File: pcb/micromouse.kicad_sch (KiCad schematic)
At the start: 15 parts, among them J1 AVR-ISP-6, U1 TSSP77038ETR, U2 TSSP77038ETR, U3 TSSP77038ETR, U4 TSSP77038ETR, U5 TSSP77038ETR, U6 TSSP77038ETR, U7 ATmega328PB-A, U8 MX1508, Y1 Crystal

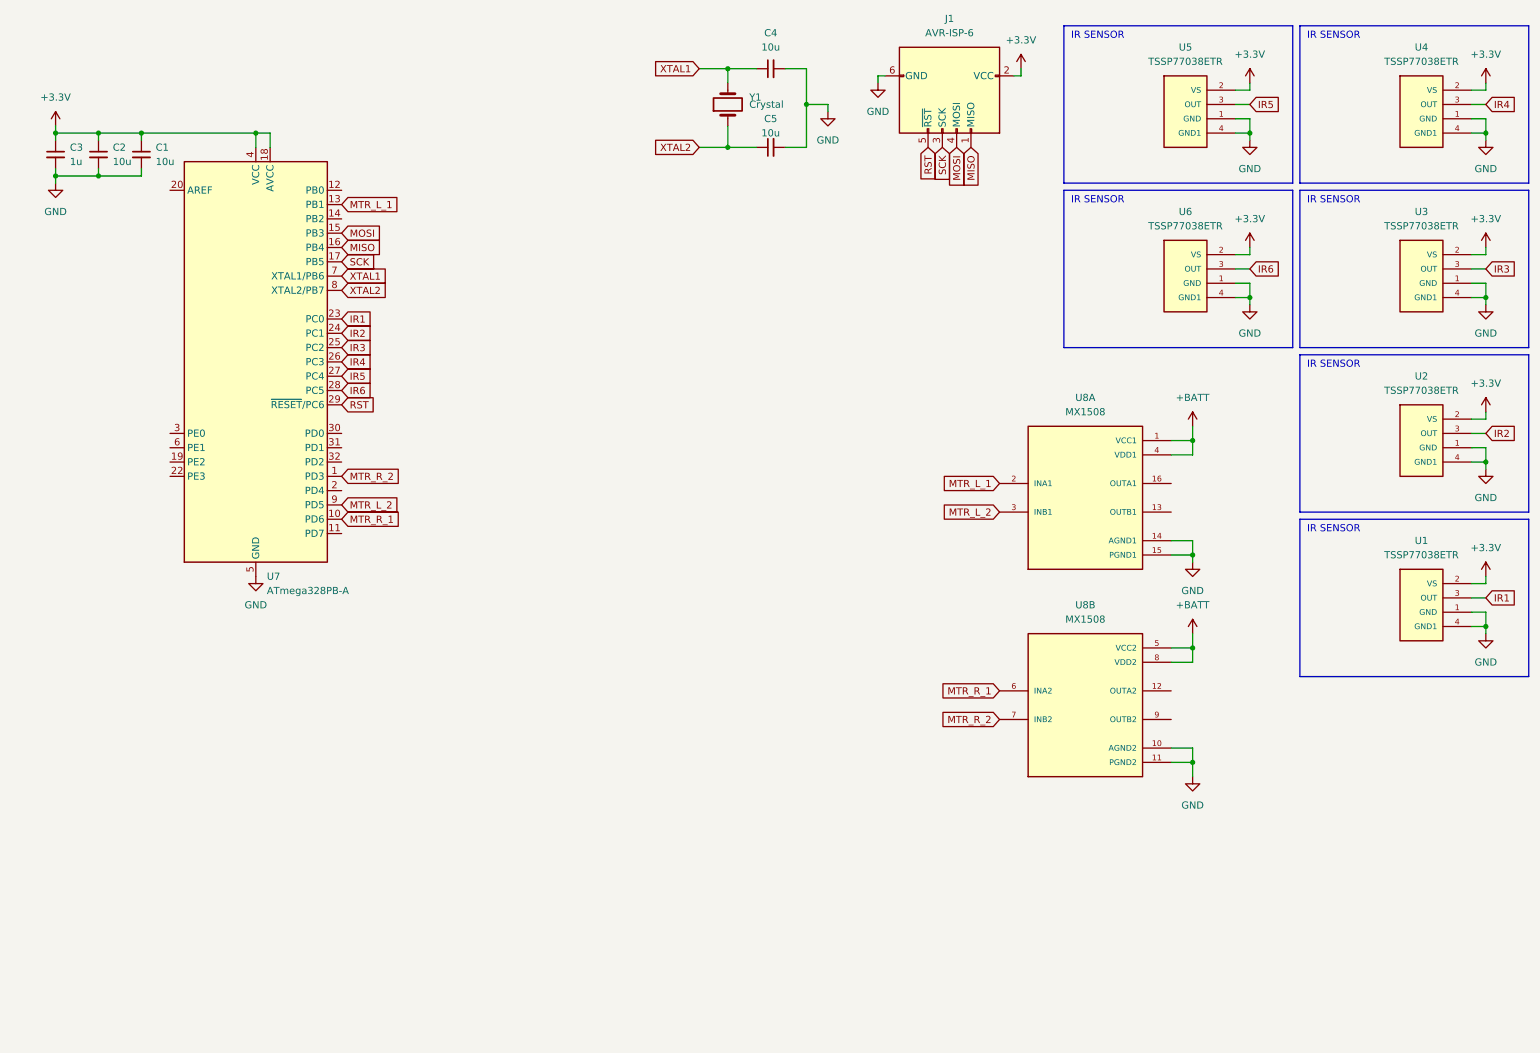
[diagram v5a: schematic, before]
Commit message: add fan control
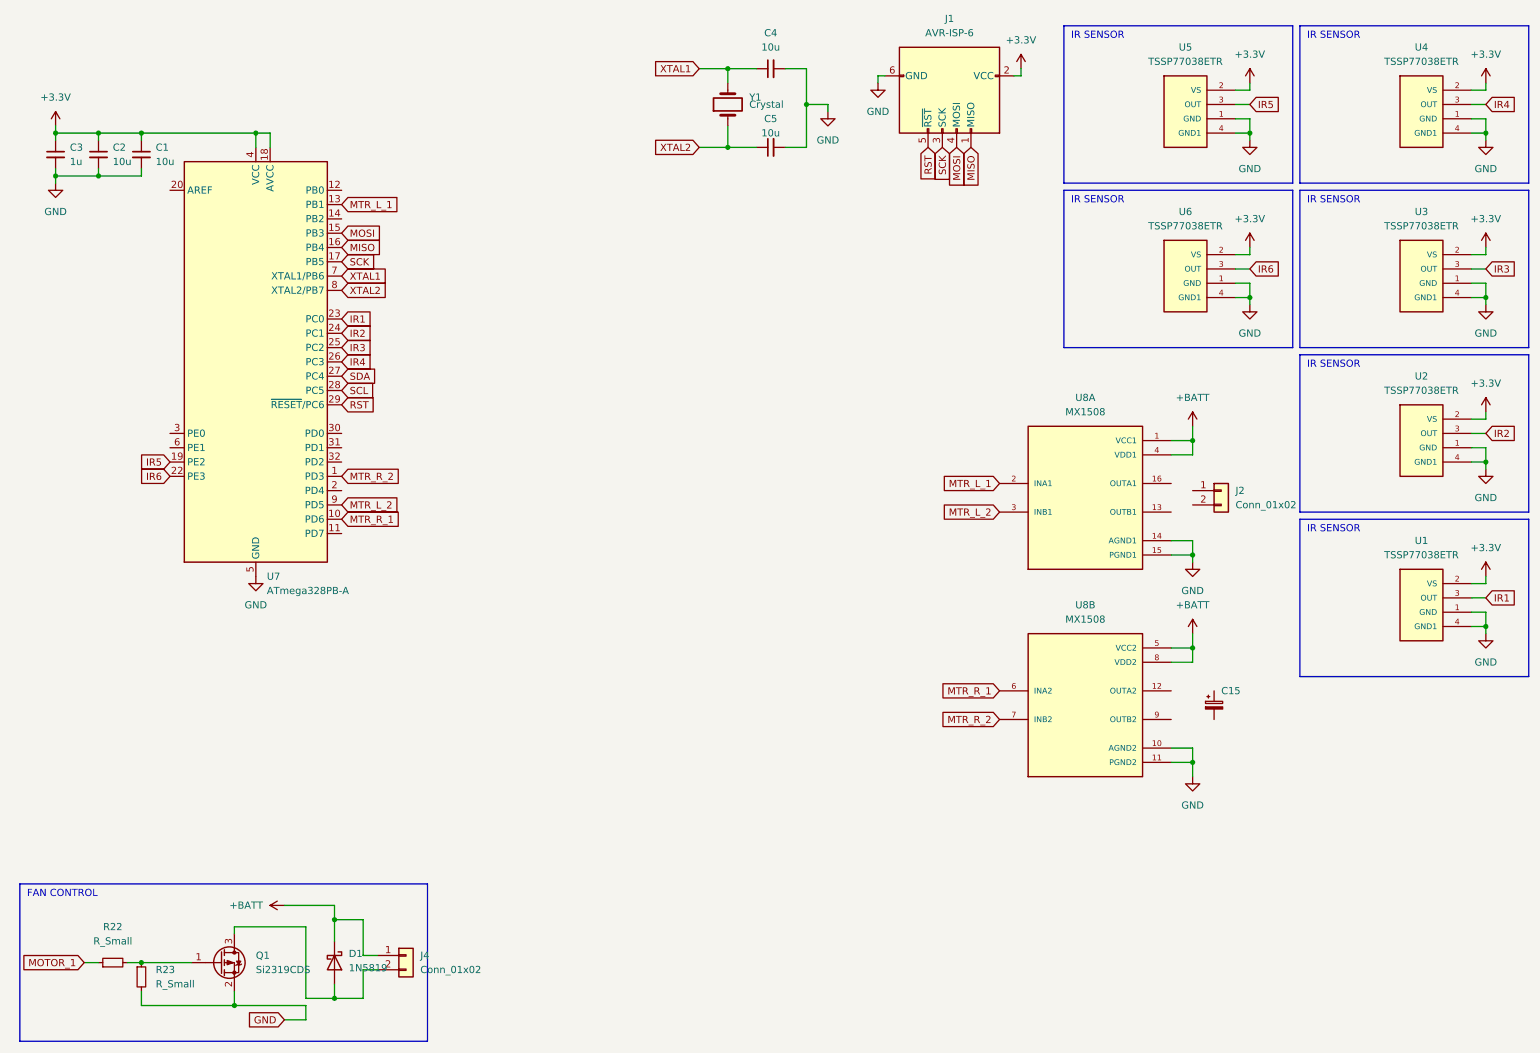
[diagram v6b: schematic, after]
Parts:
- added C15: C_Polarized_Small, Capacitor_SMD:CP_Elec_6.3x4.9, symbol Device:C_Polarized_Small
- added D1: 1N5819, Diode_THT:D_DO-41_SOD81_P10.16mm_Horizontal, symbol Diode:1N5819
- added J2: Conn_01x02, Connector_PinSocket_2.54mm:PinSocket_1x02_P2.54mm_Vertical, symbol Connector_Generic:Conn_01x02
- added J4: Conn_01x02, Connector_PinHeader_2.54mm:PinHeader_1x02_P2.54mm_Vertical, symbol Connector_Generic:Conn_01x02
- added Q1: Si2319CDS, Package_TO_SOT_SMD:SOT-23, symbol Transistor_FET:Si2319CDS
- added R22, R23: R_Small, Resistor_SMD:R_0603_1608Metric, symbol Device:R_Small
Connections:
- net +BATT: now also D1.1 (K), J4.1 (Pin_1)
- net GND: now also Q1.2 (S), R23.2
- net IR5: now also U7.19 (PE2); no longer U7.27 (PC4)
- net IR6: now also U7.22 (PE3); no longer U7.28 (PC5)
- new net: Q1.1 (G), R22.2, R23.1
- new net: D1.2 (A), J4.2 (Pin_2), Q1.3 (D)
- new net MOTOR_1: R22.1
- new net SCL: U7.28 (PC5)
- new net SDA: U7.27 (PC4)
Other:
- note added: "FAN CONTROL"

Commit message: add motor + fan
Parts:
- added C15: C_Polarized_Small, Capacitor_SMD:CP_Elec_6.3x4.9, symbol Device:C_Polarized_Small
- added J2: Conn_01x02, Connector_PinSocket_2.54mm:PinSocket_1x02_P2.54mm_Vertical, symbol Connector_Generic:Conn_01x02
- U8: footprint MX1508:SOIC127P600X177-16N -> Package_SO:SOIC-16_3.9x9.9mm_P1.27mm
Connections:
- net +BATT: now also C15.1, C15.1
- net GND: now also C15.2, C15.2
- net at U8.13 (OUTB1): now also J2.2 (Pin_2)
- net at U8.16 (OUTA1): now also J2.1 (Pin_1)
- net at U8.12 (OUTA2): now also J2.1 (Pin_1)
- net at U8.9 (OUTB2): now also J2.2 (Pin_2)
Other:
- moved on the sheet: C15
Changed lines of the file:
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@@
   (junction (at 27.94 41.91) (diameter 0) (color 0 0 0 0)
   )
+  (junction (at 228.6 138.43) (diameter 0) (color 0 0 0 0)
+  )
   (junction (at 222.25 125.73) (diameter 0) (color 0 0 0 0)
   )
@@
   (junction (at 139.7 36.83) (diameter 0) (color 0 0 0 0)
   )
+  (junction (at 228.6 133.35) (diameter 0) (color 0 0 0 0)
+  )
   (junction (at 222.25 146.05) (diameter 0) (color 0 0 0 0)
   )
@@
   (junction (at 222.25 109.22) (diameter 0) (color 0 0 0 0)
   )
+  (junction (at 222.25 128.27) (diameter 0) (color 0 0 0 0)
+  )
   (junction (at 274.32 121.92) (diameter 0) (color 0 0 0 0)
   )
@@
   (junction (at 139.7 22.86) (diameter 0) (color 0 0 0 0)
   )
+  (junction (at 222.25 143.51) (diameter 0) (color 0 0 0 0)
+  )
   (wire (pts (xy 191.77 24.13) (xy 191.77 22.86))
     (stroke (width 0) (type default))
@@
     (stroke (width 0) (type default))
   )
+  (wire (pts (xy 218.44 97.79) (xy 218.44 96.52))
+    (stroke (width 0) (type default))
+  )
   (polyline (pts (xy 86.36 195.58) (xy 86.36 167.64))
     (stroke (width 0) (type default))
@@
     (stroke (width 0) (type default))
   )
+  (wire (pts (xy 222.25 97.79) (xy 218.44 97.79))
+    (stroke (width 0) (type default))
+  )
   (wire (pts (xy 139.7 22.86) (xy 144.78 22.86))
     (stroke (width 0) (type default))
@@
     (stroke (width 0) (type default))
   )
+  (wire (pts (xy 228.6 143.51) (xy 222.25 143.51))
+    (stroke (width 0) (type default))
+  )
   (wire (pts (xy 271.78 63.5) (xy 274.32 63.5))
     (stroke (width 0) (type default))
@@
     (stroke (width 0) (type default))
   )
+  (wire (pts (xy 228.6 138.43) (xy 234.95 138.43))
+    (stroke (width 0) (type default))
+  )
   (wire (pts (xy 52.07 189.23) (xy 64.77 189.23))
     (stroke (width 0) (type default))
@@
     (stroke (width 0) (type default))
   )
+  (wire (pts (xy 218.44 100.33) (xy 218.44 101.6))
+    (stroke (width 0) (type default))
+  )
   (wire (pts (xy 232.41 26.67) (xy 232.41 25.4))
     (stroke (width 0) (type default))
@@
     (stroke (width 0) (type default))
   )
+  (wire (pts (xy 222.25 100.33) (xy 218.44 100.33))
+    (stroke (width 0) (type default))
+  )
   (wire (pts (xy 149.86 22.86) (xy 153.67 22.86))
     (stroke (width 0) (type default))
@@
     (stroke (width 0) (type default))
   )
+  (wire (pts (xy 228.6 138.43) (xy 228.6 143.51))
+    (stroke (width 0) (type default))
+  )
   (wire (pts (xy 232.41 55.88) (xy 232.41 54.61))
     (stroke (width 0) (type default))
   )
+  (wire (pts (xy 219.71 137.16) (xy 218.44 137.16))
+    (stroke (width 0) (type default))
+  )
   (wire (pts (xy 218.44 106.68) (xy 222.25 106.68))
     (stroke (width 0) (type default))
@@
     (stroke (width 0) (type default))
   )
+  (wire (pts (xy 219.71 134.62) (xy 218.44 134.62))
+    (stroke (width 0) (type default))
+  )
   (wire (pts (xy 232.41 31.75) (xy 232.41 34.29))
     (stroke (width 0) (type default))
@@
     (stroke (width 0) (type default))
   )
+  (wire (pts (xy 222.25 128.27) (xy 228.6 128.27))
+    (stroke (width 0) (type default))
+  )
   (wire (pts (xy 274.32 92.71) (xy 274.32 93.98))
     (stroke (width 0) (type default))
@@
     (stroke (width 0) (type default))
   )
+  (wire (pts (xy 228.6 128.27) (xy 228.6 133.35))
+    (stroke (width 0) (type default))
+  )
   (wire (pts (xy 274.32 31.75) (xy 274.32 34.29))
     (stroke (width 0) (type default))
@@
     (stroke (width 0) (type default))
   )
+  (wire (pts (xy 228.6 133.35) (xy 234.95 133.35))
+    (stroke (width 0) (type default))
+  )
   (wire (pts (xy 222.25 146.05) (xy 222.25 148.59))
     (stroke (width 0) (type default))
@@
     (stroke (width 0) (type default))
   )
+  (wire (pts (xy 218.44 134.62) (xy 218.44 133.35))
+    (stroke (width 0) (type default))
+  )
   (wire (pts (xy 134.62 22.86) (xy 139.7 22.86))
     (stroke (width 0) (type default))
@@
   )
   (wire (pts (xy 69.85 173.99) (xy 74.93 173.99))
+    (stroke (width 0) (type default))
+  )
+  (wire (pts (xy 218.44 137.16) (xy 218.44 138.43))
     (stroke (width 0) (type default))
   )
@@
     )
   )
+  (symbol (lib_id "Device:C_Polarized_Small") (at 234.95 135.89 0) (unit 1)
+    (in_bom yes) (on_board yes) (dnp no)
+    (property "Reference" "C15" (at 236.22 133.35 0)
+      (effects (font (size 1.27 1.27)) (justify left))
+    )
+    (property "Value" "C_Polarized_Small" (at 237.49 136.6139 0)
+      (effects (font (size 1.27 1.27)) (justify left) hide)
+    )
+    (property "Footprint" "Capacitor_SMD:CP_Elec_6.3x4.9" (at 234.95 135.89 0)
+      (effects (font (size 1.27 1.27)) hide)
+    )
+    (property "Datasheet" "~" (at 234.95 135.89 0)
+      (effects (font (size 1.27 1.27)) hide)
+    )
+    (pin "1")
+    (pin "2")
+    (instances
+      (project "line-follower"
+        (path "/16c7c831-eafb-4a0a-afab-2bf2c115b426"
+          (reference "C15") (unit 1)
+        )
+      )
+      (project "micromouse"
+        (path "/405a5ba7-3106-45d0-abc8-375c92cb441a"
+          (reference "C6") (unit 1)
+        )
+      )
+      (project "robot-lidar"
+        (path "/cb10bbf7-c2c1-4a0d-8947-ad707931d83b"
+          (reference "C23") (unit 1)
+        )
+      )
+    )
+  )
   (symbol (lib_id "power:GND") (at 274.32 64.77 0) (unit 1)
     (in_bom yes) (on_board yes) (dnp no) (fields_autoplaced)
@@
     )
   )
-  (symbol (lib_id "Device:C_Polarized_Small") (at 226.06 135.89 0) (unit 1)
+  (symbol (lib_id "Device:C_Polarized_Small") (at 228.6 135.89 0) (unit 1)
     (in_bom yes) (on_board yes) (dnp no)
-    (property "Reference" "C15" (at 227.33 133.35 0)
+    (property "Reference" "C15" (at 229.87 133.35 0)
       (effects (font (size 1.27 1.27)) (justify left))
     )
-    (property "Value" "C_Polarized_Small" (at 228.6 136.6139 0)
-      (effects (font (size 1.27 1.27)) (justify left) hide)
-    )
-    (property "Footprint" "Capacitor_SMD:CP_Elec_6.3x4.9" (at 226.06 135.89 0)
-      (effects (font (size 1.27 1.27)) hide)
-    )
-    (property "Datasheet" "~" (at 226.06 135.89 0)
+    (property "Value" "C_Polarized_Small" (at 231.14 136.6139 0)
+      (effects (font (size 1.27 1.27)) (justify left) hide)
+    )
+    (property "Footprint" "Capacitor_SMD:CP_Elec_6.3x4.9" (at 228.6 135.89 0)
+      (effects (font (size 1.27 1.27)) hide)
+    )
+    (property "Datasheet" "~" (at 228.6 135.89 0)
       (effects (font (size 1.27 1.27)) hide)
     )
@@
       (effects (font (size 1.27 1.27)))
     )
-    (property "Footprint" "MX1508:SOIC127P600X177-16N" (at 203.2 99.06 0)
+    (property "Footprint" "Package_SO:SOIC-16_3.9x9.9mm_P1.27mm" (at 203.2 99.06 0)
       (effects (font (size 1.27 1.27)) (justify bottom) hide)
     )
@@
       (effects (font (size 1.27 1.27)))
     )
-    (property "Footprint" "MX1508:SOIC127P600X177-16N" (at 203.2 135.89 0)
+    (property "Footprint" "Package_SO:SOIC-16_3.9x9.9mm_P1.27mm" (at 203.2 135.89 0)
       (effects (font (size 1.27 1.27)) (justify bottom) hide)
     )
@@
         )
       )
+    )
+  )
+  (symbol (lib_id "Connector_Generic:Conn_01x02") (at 224.79 134.62 0) (unit 1)
+    (in_bom yes) (on_board yes) (dnp no)
+    (property "Reference" "J2" (at 227.33 134.62 0)
+      (effects (font (size 1.27 1.27)) (justify left))
+    )
+    (property "Value" "Conn_01x02" (at 219.71 139.7 0)
+      (effects (font (size 1.27 1.27)) (justify left))
+    )
+    (property "Footprint" "Connector_PinSocket_2.54mm:PinSocket_1x02_P2.54mm_Vertical" (at 224.79 134.62 0)
+      (effects (font (size 1.27 1.27)) hide)
+    )
+    (property "Datasheet" "~" (at 224.79 134.62 0)
+      (effects (font (size 1.27 1.27)) hide)
+    )
+    (pin "1")
+    (pin "2")
+    (instances
+      (project "line-follower"
+        (path "/16c7c831-eafb-4a0a-afab-2bf2c115b426"
+          (reference "J2") (unit 1)
+        )
+      )
+      (project "micromouse"
+        (path "/405a5ba7-3106-45d0-abc8-375c92cb441a"
+          (reference "J3") (unit 1)
+        )
+      )
+      (project "robot-lidar"
+        (path "/cb10bbf7-c2c1-4a0d-8947-ad707931d83b"
+          (reference "J7") (unit 1)
+        )
+      )
